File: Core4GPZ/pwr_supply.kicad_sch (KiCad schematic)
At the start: 3 parts

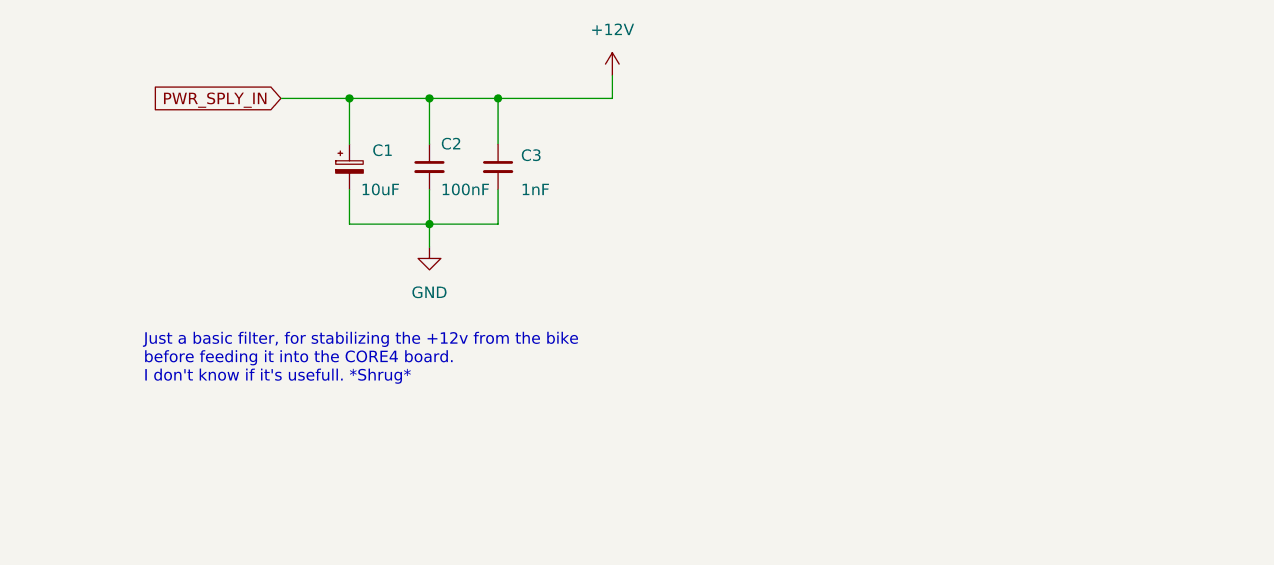
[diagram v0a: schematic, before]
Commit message: Changed Connectors for Molex CMC 48pins Black.
Changed ECU Connector for Molex CMC 48pins Black, for compacity and cost reduction. Designed custom Footprint for this purpose
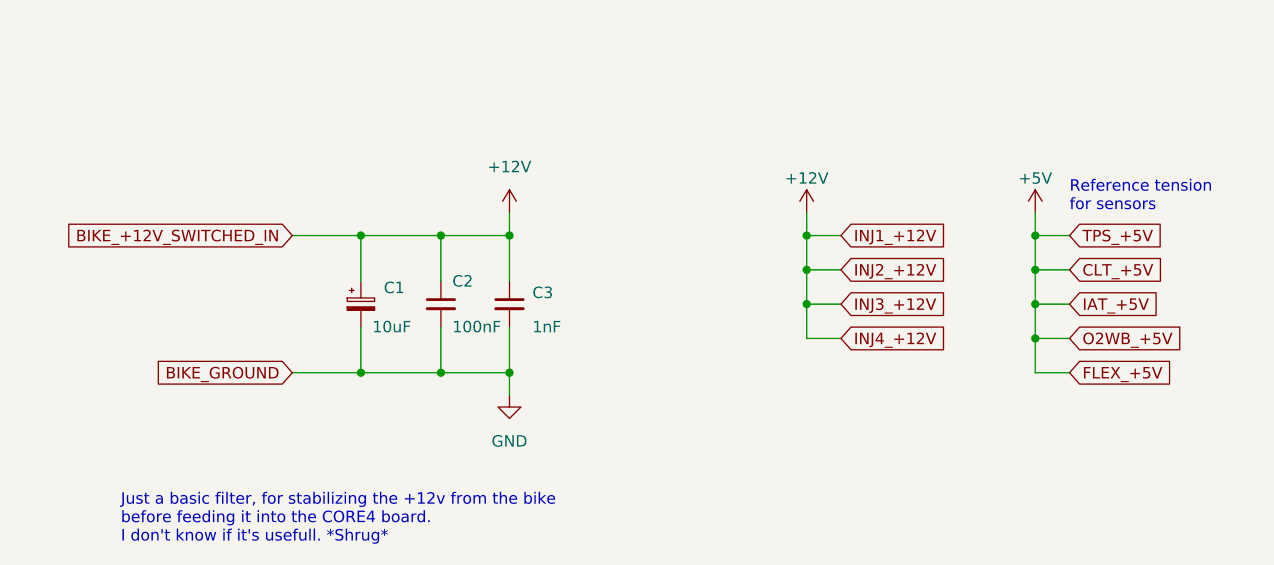
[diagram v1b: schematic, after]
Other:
- note added: "Reference tension for sensors"
- moved on the sheet: C1, C2, C3

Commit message: Test montage générateur de Haute tension
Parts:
- C2, C3: footprint Capacitor_THT:C_Rect_L7.0mm_W2.5mm_P5.00mm -> Capacitor_SMD:C_1206_3216Metric_Pad1.33x1.80mm_HandSolder
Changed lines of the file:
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@@
       (effects (font (size 1.27 1.27)) (justify left))
     )
-    (property "Footprint" "Capacitor_THT:C_Rect_L7.0mm_W2.5mm_P5.00mm" (at 64.77 52.07 0)
+    (property "Footprint" "Capacitor_SMD:C_1206_3216Metric_Pad1.33x1.80mm_HandSolder" (at 64.77 52.07 0)
       (effects (font (size 1.27 1.27)) hide)
     )
@@
       (effects (font (size 1.27 1.27)) (justify left))
     )
-    (property "Footprint" "Capacitor_THT:C_Rect_L7.0mm_W2.5mm_P5.00mm" (at 72.39 52.07 0)
+    (property "Footprint" "Capacitor_SMD:C_1206_3216Metric_Pad1.33x1.80mm_HandSolder" (at 72.39 52.07 0)
       (effects (font (size 1.27 1.27)) hide)
     )

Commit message: Started Implementation of VR Conditionner
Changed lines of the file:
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@@
-	)
-	(junction
-		(at 105.41 48.26)
-		(diameter 0)
-		(color 0 0 0 0)
 	)
 	(junction
@@
 		(color 0 0 0 0)
 	)
-	(junction
-		(at 105.41 52.07)
-		(diameter 0)
-		(color 0 0 0 0)
-	)
-	(junction
-		(at 105.41 44.45)
-		(diameter 0)
-		(color 0 0 0 0)
-	)
 	(wire
 		(pts
@@
 	(wire
 		(pts
+			(xy 72.39 44.45) (xy 77.47 44.45)
+		)
+		(stroke
+			(width 0)
+			(type default)
+		)
+	)
+	(wire
+		(pts
 			(xy 130.81 41.91) (xy 130.81 44.45)
 		)
@@
 	(wire
 		(pts
-			(xy 105.41 48.26) (xy 105.41 52.07)
-		)
-		(stroke
-			(width 0)
-			(type default)
-		)
-	)
-	(wire
-		(pts
-			(xy 105.41 55.88) (xy 109.22 55.88)
-		)
-		(stroke
-			(width 0)
-			(type default)
-		)
-	)
-	(wire
-		(pts
-			(xy 105.41 48.26) (xy 109.22 48.26)
-		)
-		(stroke
-			(width 0)
-			(type default)
-		)
-	)
-	(wire
-		(pts
-			(xy 105.41 52.07) (xy 105.41 55.88)
-		)
-		(stroke
-			(width 0)
-			(type default)
-		)
-	)
-	(wire
-		(pts
 			(xy 130.81 44.45) (xy 134.62 44.45)
 		)
@@
 	(wire
 		(pts
-			(xy 105.41 41.91) (xy 105.41 44.45)
-		)
-		(stroke
-			(width 0)
-			(type default)
-		)
-	)
-	(wire
-		(pts
 			(xy 72.39 59.69) (xy 72.39 54.61)
 		)
@@
 	(wire
 		(pts
-			(xy 105.41 44.45) (xy 109.22 44.45)
-		)
-		(stroke
-			(width 0)
-			(type default)
-		)
-	)
-	(wire
-		(pts
 			(xy 55.88 44.45) (xy 55.88 49.53)
 		)
@@
 	(wire
 		(pts
-			(xy 105.41 44.45) (xy 105.41 48.26)
-		)
-		(stroke
-			(width 0)
-			(type default)
-		)
-	)
-	(wire
-		(pts
 			(xy 64.77 44.45) (xy 72.39 44.45)
 		)
@@
 		(pts
 			(xy 130.81 55.88) (xy 134.62 55.88)
-		)
-		(stroke
-			(width 0)
-			(type default)
-		)
-	)
-	(wire
-		(pts
-			(xy 105.41 52.07) (xy 109.22 52.07)
 		)
 		(stroke
@@
 		)
 	)
-	(global_label "INJ4_+12V"
+	(global_label "INJ_+12V"
 		(shape input)
-		(at 109.22 55.88 0)
+		(at 77.47 44.45 0)
 		(fields_autoplaced yes)
 		(effects
@@
 		)
 		(property "Intersheetrefs" "${INTERSHEET_REFS}"
-			(at 122.3652 55.88 0)
-			(effects
-				(font
-					(size 1.27 1.27)
-				)
-				(justify left)
-				(hide yes)
-			)
-		)
-	)
-	(global_label "INJ1_+12V"
-		(shape input)
-		(at 109.22 44.45 0)
-		(fields_autoplaced yes)
-		(effects
-			(font
-				(size 1.27 1.27)
-			)
-			(justify left)
-		)
-		(property "Intersheetrefs" "${INTERSHEET_REFS}"
-			(at 122.3652 44.45 0)
-			(effects
-				(font
-					(size 1.27 1.27)
-				)
-				(justify left)
-				(hide yes)
-			)
-		)
-	)
-	(global_label "INJ2_+12V"
-		(shape input)
-		(at 109.22 48.26 0)
-		(fields_autoplaced yes)
-		(effects
-			(font
-				(size 1.27 1.27)
-			)
-			(justify left)
-		)
-		(property "Intersheetrefs" "${INTERSHEET_REFS}"
-			(at 122.3652 48.26 0)
+			(at 89.4057 44.45 0)
 			(effects
 				(font
@@
 		(property "Intersheetrefs" "${INTERSHEET_REFS}"
 			(at 145.1043 52.07 0)
-			(effects
-				(font
-					(size 1.27 1.27)
-				)
-				(justify left)
-				(hide yes)
-			)
-		)
-	)
-	(global_label "INJ3_+12V"
-		(shape input)
-		(at 109.22 52.07 0)
-		(fields_autoplaced yes)
-		(effects
-			(font
-				(size 1.27 1.27)
-			)
-			(justify left)
-		)
-		(property "Intersheetrefs" "${INTERSHEET_REFS}"
-			(at 122.3652 52.07 0)
 			(effects
 				(font
@@
 					(unit 1)
 				)
-			)
-		)
-	)
-	(symbol
-		(lib_id "power:+12V")
-		(at 105.41 41.91 0)
-		(unit 1)
-		(exclude_from_sim no)
-		(in_bom yes)
-		(on_board yes)
-		(dnp no)
-		(property "Reference" "#PWR08"
-			(at 105.41 45.72 0)
-			(effects
-				(font
-					(size 1.27 1.27)
-				)
-				(hide yes)
-			)
-		)
-		(property "Value" "+12V"
-			(at 105.41 38.1 0)
-			(effects
-				(font
-					(size 1.27 1.27)
-				)
-			)
-		)
-		(property "Footprint" ""
-			(at 105.41 41.91 0)
-			(effects
-				(font
-					(size 1.27 1.27)
-				)
-				(hide yes)
-			)
-		)
-		(property "Datasheet" ""
-			(at 105.41 41.91 0)
-			(effects
-				(font
-					(size 1.27 1.27)
-				)
-				(hide yes)
-			)
-		)
-		(property "Description" ""
-			(at 105.41 41.91 0)
-			(effects
-				(font
-					(size 1.27 1.27)
-				)
-				(hide yes)
-			)
-		)
-		(pin "1"
-		)
-		(instances
-			(project "Core4GPZ"
-				(path "/ac28f42d-34b3-4fcc-84dd-ab6106f99610/daf77dd8-6c93-40bb-b740-2abe26fd61d2"
-					(reference "#PWR08")
-					(unit 1)
-				)
